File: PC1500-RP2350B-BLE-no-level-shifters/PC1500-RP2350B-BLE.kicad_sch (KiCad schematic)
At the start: 40 parts, among them J1 microSD, J2 USB-C (programming/debug), J3 PC-1500 40-pin cartridge slot, J5 PC1500_SENSE_JUMPER, J6 SPARE_GPIO_U9, J7 SWD_I2C_HEADER, SW1 BOOTSEL, U1 RP2354B, U10 TCA9406DCUR, U2 AS6C62256-55STCN, U3 SLG46826V, U4 AP2112K-3.3, U8 RN4871, U9 SLG46826V, X1 12MHz (Abracon ABM8-272-T3)

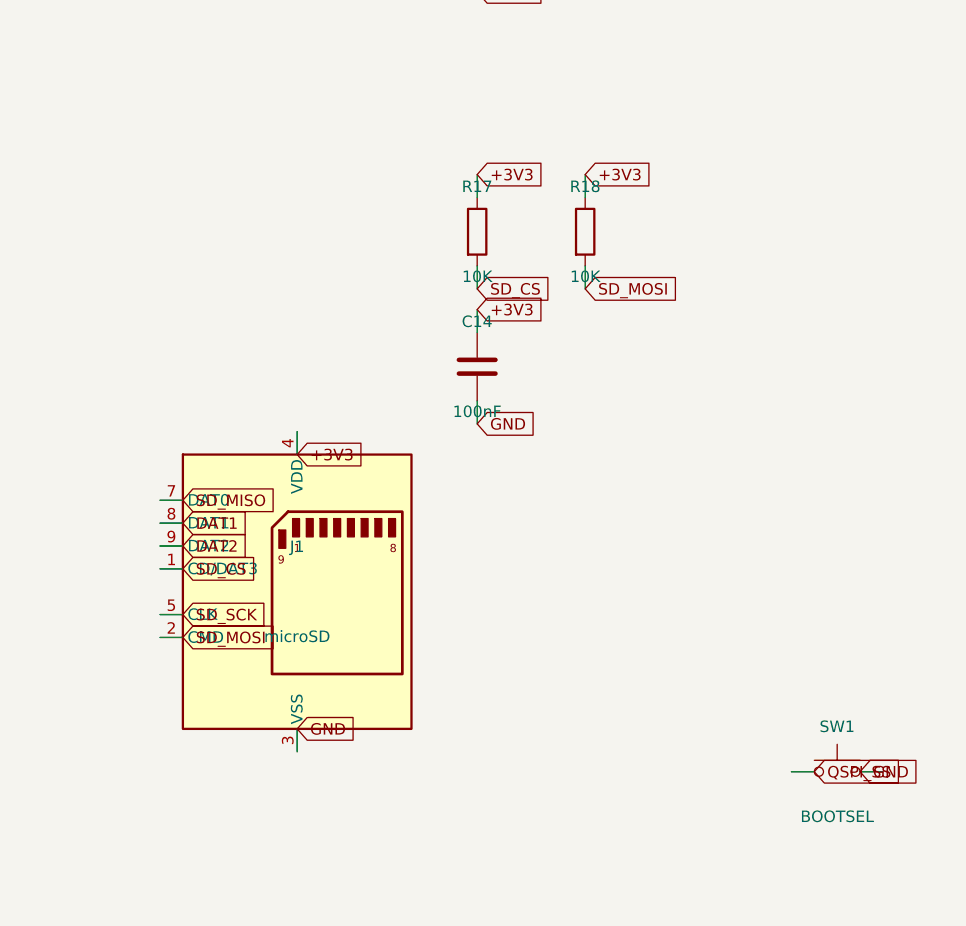
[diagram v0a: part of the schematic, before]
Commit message: Fix microSD pin 6 (GND) and pin 1 (unused, needs pull-up) on all 4 boards
Pin 6 and pin 3 were coincident in the generic SD_Card_Device symbol,
forcing GND onto the same net as CMD/MOSI. Relocated pin 6's local
coordinate and gave it its own wire+label on all four schematics
(RP2350B-BLE and Pico2W-Dongle, each with and without level shifters).

Pin 1 (symbol name CD/DAT3) is unused in this design but needs a 10K
pull-up to 3.3V rather than being left floating, matching the existing
SD_CS/SD_MOSI/SD_DAT1/SD_DAT2 pull-up pattern. Added the missing
wire+label+resistor to the three boards that lacked it
(Pico2W-Dongle-no-level-shifters already had it via R10).

Co-Authored-By: Claude Sonnet 5 <noreply@anthropic.com>
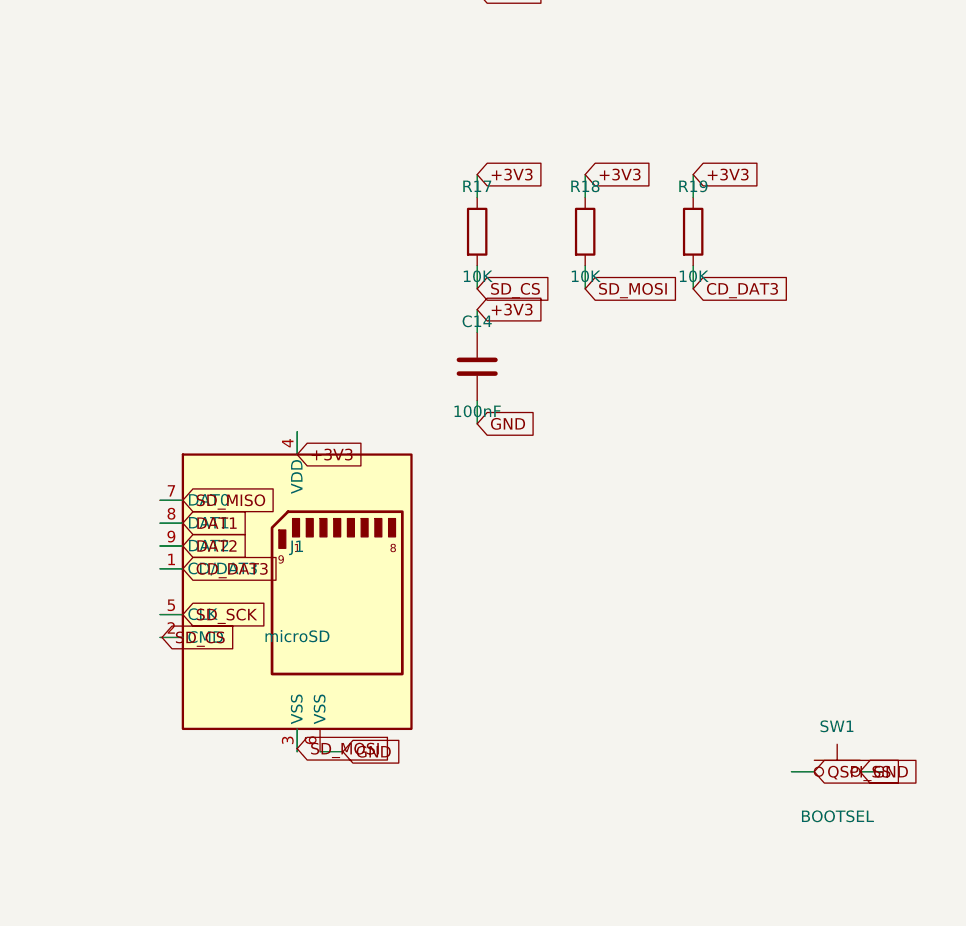
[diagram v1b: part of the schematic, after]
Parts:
- added R19: 10K, Resistor_SMD:R_0201_0603Metric, symbol Device:R
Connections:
- net +3V3: now also R19.1
- net GND: no longer J1.3 (VSS)
- net SD_CS: now also J1.2 (CMD); no longer J1.1 (CD/DAT3)
- net SD_MOSI: now also J1.3 (VSS); no longer J1.2 (CMD)
- new net CD_DAT3: J1.1 (CD/DAT3), R19.2

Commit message: Boards: card-edge pinout and X1 fixes; More-RAM, ROM replacement, adapter
- Card edge (J3), all boards: viewed from the top with the edge up,
  pin 1 is on the right, 21 under 1, 40 under 20. The pads were mirrored;
  fixed in place, no rerouting.
- X1 (ABM8): the 4-pad crystal had the 2-pin Device:Crystal symbol. Now
  Device:Crystal_GND24 (XIN 1, XOUT 3, GND 2/4) on More-RAM and both
  RP2350B-BLE boards.
- PC1500-RP2354B-BLE-more-RAM (the internal card), new in git:
  - BGM220SC22WGA2 replaces the RN4871: footprint from datasheet Rev 1.4
    with the antenna loop on ANT_OUT, no copper under the antenna or its
    keepout, a ground pour around the module only, thermal-relief centre
    pads; R24 0R between ANT_IN and RF_2G4.
  - D0-D7 on GPIO16-23 in order (the PIO window); GREENPAK2_IO14 on
    GPIO25 (5 V tolerant); UART0 GPIO32-35, RESETn 36, HOST_WAKE 37,
    SWD 38/39, BLE_MODULE_WAKE GPIO27 -> PB03.
  - SD_MISO reconnected to GPIO40 (a label 1.27 mm off the pin end).
  - Signal netclass for every signal net.
- PC1500-ROM-Replacement-Board and PC-1500-40-pin-Breadboard-Adapter
  (Sullins RBB20DHHN socket, DIP-40 and DIP-28 hole rows), new in git.
- .gitignore: scripted-edit backups, KiCad history and editor locks.

Design files only: fab/production outputs aren't included (More-RAM's
fab/ predates these changes).

Co-Authored-By: Claude Opus 5.5 <noreply@anthropic.com>
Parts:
- X1: symbol Device:Crystal -> Device:Crystal_GND24
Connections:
- net D5: now also U2.17 (Q5)
- net GND: now also X1.2 (G), X1.4 (G)
- net GREENPAK2_IO14: now also U9.20 (IO14)
- net SRAM_A11: now also U3.10 (IO6)
- net SRAM_A12: now also U3.12 (IO7)
- net XOUT: now also X1.3; no longer X1.2
- net GREENPAK1_SCL renamed SCL
- net GREENPAK1_SDA renamed SDA
